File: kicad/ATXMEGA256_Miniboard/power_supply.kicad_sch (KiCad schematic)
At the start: 9 parts, among them J14 1x3 Goldpin Header, J15 1x3 Goldpin Header, J16 1x2 Goldpin Header, J17 1x2 Goldpin Header, U2 MCP1703A-3302E_DB

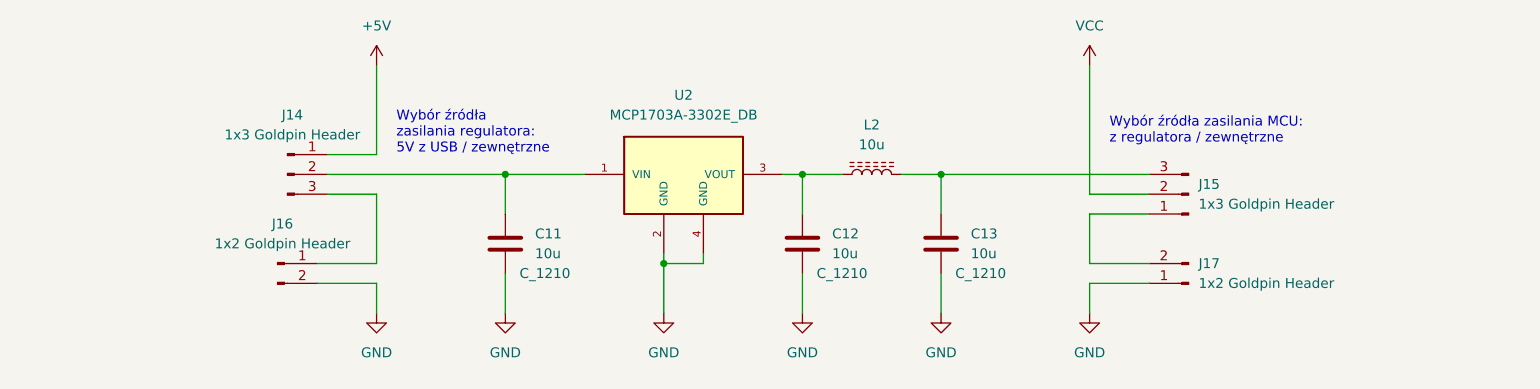
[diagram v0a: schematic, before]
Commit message: led + złącze masy + złącze śrubowe (do opisania)
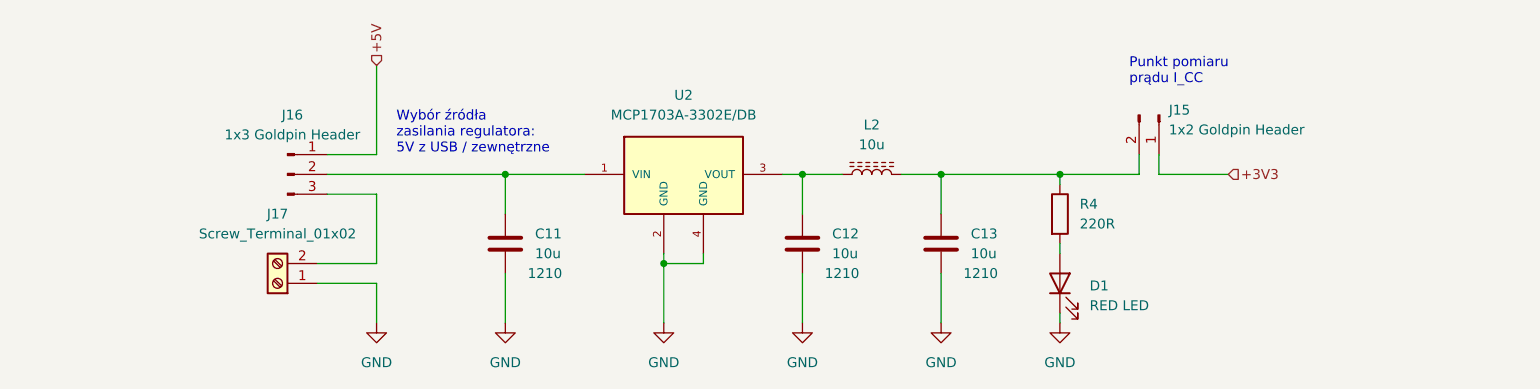
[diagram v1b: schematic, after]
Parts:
- removed J15: 1x3 Goldpin Header, Connector_PinHeader_2.54mm:PinHeader_1x03_P2.54mm_Vertical, symbol Connector:Conn_01x03_Pin
- removed J16, J17: 1x2 Goldpin Header, Connector_PinHeader_2.54mm:PinHeader_1x02_P2.54mm_Vertical, symbol Connector:Conn_01x02_Pin
- added D1: RED LED, LED_SMD:LED_0805_2012Metric_Pad1.15x1.40mm_HandSolder, symbol Device:LED
- added J15: 1x2 Goldpin Header, Connector_PinHeader_2.54mm:PinHeader_1x02_P2.54mm_Vertical, symbol Connector:Conn_01x02_Pin
- added J17: Screw_Terminal_01x02, symbol Connector:Screw_Terminal_01x02
- added R4: 220R, Resistor_SMD:R_0603_1608Metric_Pad0.98x0.95mm_HandSolder, symbol Device:R
- C11, C12, C13: Package C_1210 -> 1210
- U2: value MCP1703A-3302E_DB -> MCP1703A-3302E/DB
- renumbered J14 to J16
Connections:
- net GND: now also D1.1 (K), J17.1 (Pin_1)
- net at C13.2, L2.2: now also J15.2 (Pin_2), R4.1
- net at J16.3 (Pin_3): now also J17.2 (Pin_2)
- new net: D1.2 (A), R4.2
- new net +3V3: J15.1 (Pin_1)
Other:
- note added: "Punkt pomiaru prądu I_CC"
- note removed: "Wybór źródła zasilania MCU: z regulatora / zewnętrzne"

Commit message: poprawka estetyczna zasilania
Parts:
- removed C13: 10u, Capacitor_SMD:C_1210_3225Metric_Pad1.33x2.70mm_HandSolder, symbol Device:C
- removed J17: Screw_Terminal_01x02, symbol Connector:Screw_Terminal_01x02
- removed L2: 10u, symbol Device:L_Ferrite
- U2: footprint MCP1703A-3302E_DB:SOT230P700X180-4N -> MCP1703A-3302E:SOT230P700X180-4N
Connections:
- net at C12.2, U2.3 (VOUT): now also J15.2 (Pin_2), R4.1
- net EXT_VCC: now reaches J16.3 (Pin_3)
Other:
- moved on the sheet: D1, J15, R4

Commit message: dorobiony tranzsytor zabezpieczajacy i dlawik
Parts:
- added C13: 10u, Capacitor_SMD:C_1210_3225Metric_Pad1.33x2.70mm_HandSolder, symbol Device:C
- added J18: 1x2 Goldpin Header, Connector_PinHeader_2.54mm:PinHeader_1x02_P2.54mm_Vertical, symbol Connector:Conn_01x02_Pin
- added L2: 10u, Inductor_SMD:L_0805_2012Metric_Pad1.15x1.40mm_HandSolder, symbol Device:L_Ferrite
- added Q1: YJL2301D, Package_TO_SOT_SMD:SOT-23, symbol Simulation_SPICE:PMOS
- added R5: 10K, symbol Device:R
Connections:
- net +3V3: now also L2.1
- net GND: now also C13.1, R5.2
- net at C11.2, U2.1 (VIN): now also Q1.2 (S); no longer J16.2 (Pin_2)
- new net: Q1.1 (G), R5.1
- new net: J16.2 (Pin_2), Q1.3 (D)
- new net: C13.2, J18.2 (Pin_2), L2.2
- new net +3V3_MCU: J18.1 (Pin_1)
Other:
- note added: "Punkt pomiaru prądu I_CC MCU"
- note added: "do zadrutowania w razie braku elementu"
- moved on the sheet: J16
